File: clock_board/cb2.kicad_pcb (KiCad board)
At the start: 2 copper layers, 110.5 x 38.1 mm, 42 parts, among them IC1 ATMEGA328-P, P1 POWER, P2 PROGRAMMER, P3 BATT_CONN, P4 LEDB_POWER, P5 LCD_CLK_CONN, P6 DIGIT_POWER, Q1 DGT1, Q2 DGT2, Q3 DGT3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

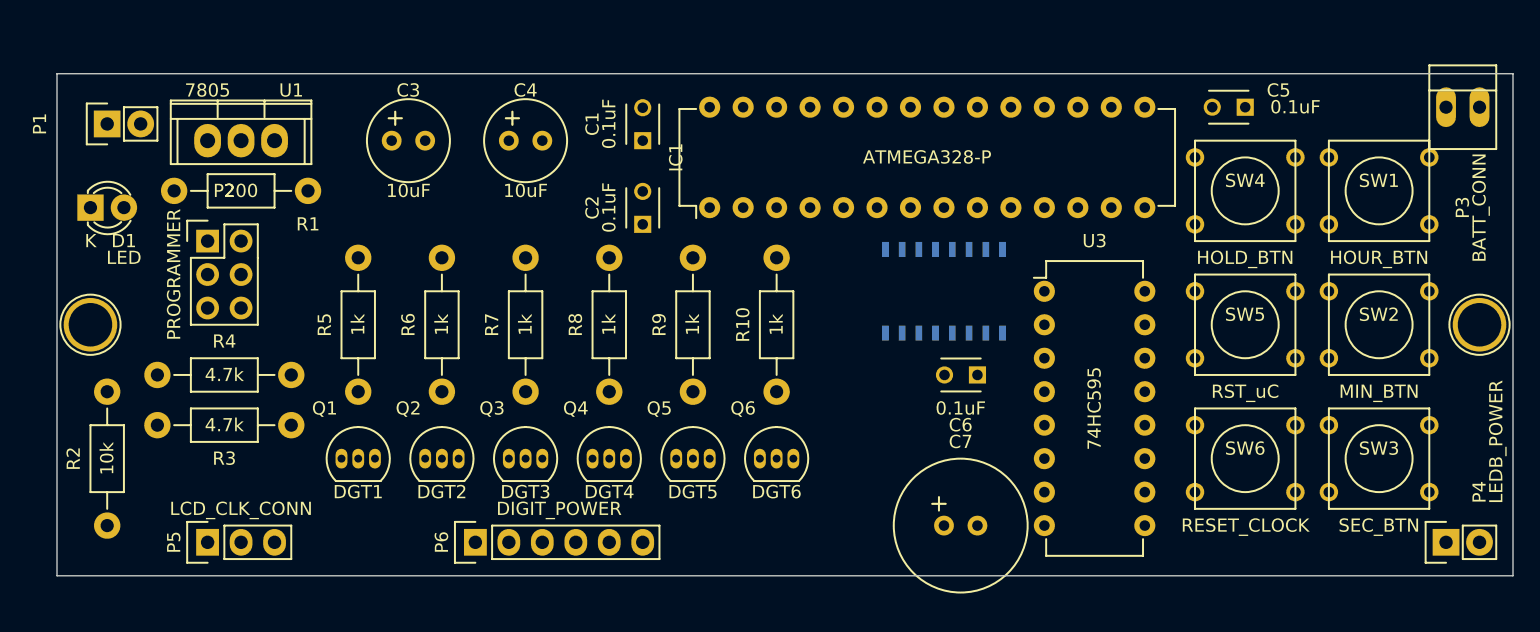
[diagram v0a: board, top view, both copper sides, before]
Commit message: Removed clock reset button.  Improved PCB layout.
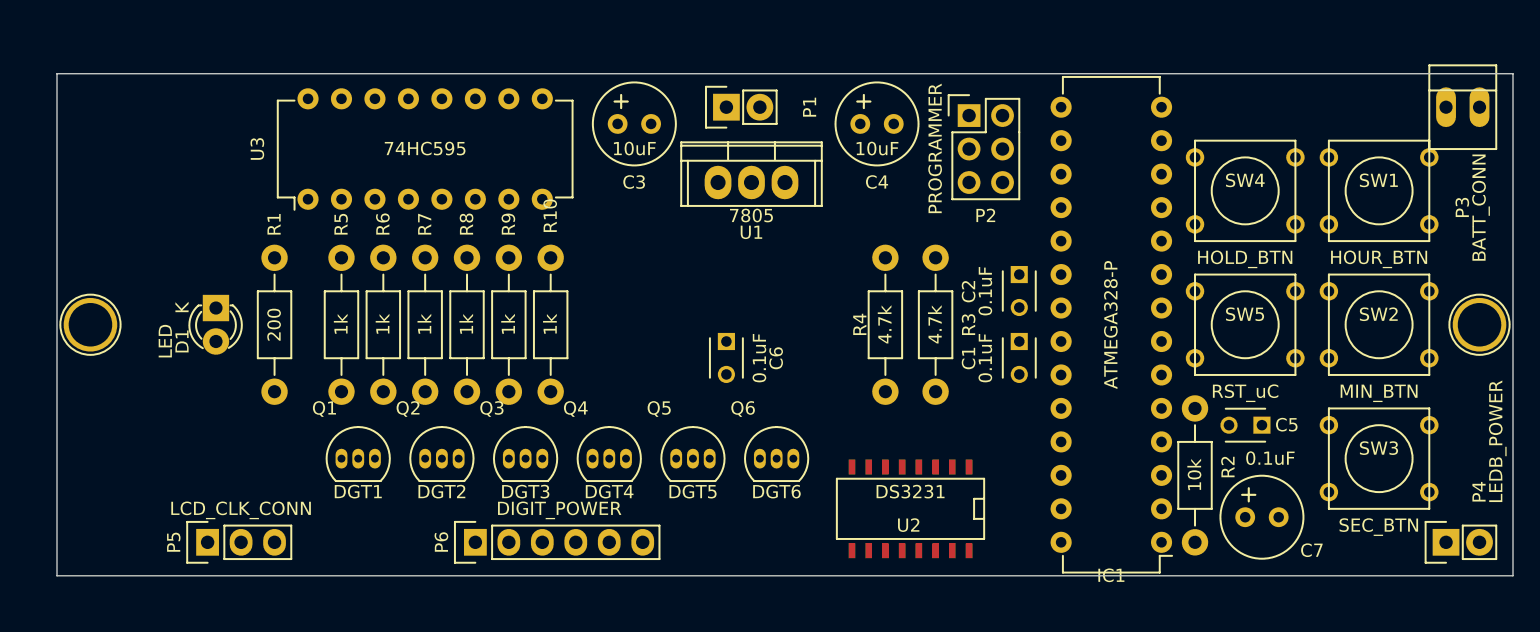
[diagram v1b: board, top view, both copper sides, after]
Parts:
- removed SW6: RESET_CLOCK, Buttons_Switches_ThroughHole:SW_PUSH_SMALL
- C7: footprint Capacitors_Elko_ThroughHole:Elko_vert_20x10mm_RM2.5 -> Capacitors_Elko_ThroughHole:Elko_vert_11.2x6.3mm_RM2.5
- U2: moved to F.Cu
- moved R2 82.6 mm to (152.4, 132.1), turned to 270 degrees
- moved P2 58.6 mm to (135.3, 104.8)
- moved U3 56.3 mm to (85.1, 111.1), turned to 90 degrees
- moved R4 54.1 mm to (132.7, 120.7), turned to 270 degrees
- moved R3 50.7 mm to (128.9, 120.7), turned to 270 degrees
- moved P1 47.0 mm to (116.8, 104.1)
- moved IC1 42.7 mm to (149.9, 137.2), turned to 180 degrees
- moved U1 38.9 mm to (118.7, 109.9)
- moved C1 32.4 mm to (139.1, 121.9), turned to 270 degrees
- moved C2 28.8 mm to (139.1, 116.8), turned to 270 degrees
- moved C4 26.7 mm to (127.0, 105.4)
- moved C5 24.2 mm to (157.5, 128.3)
- moved C7 22.9 mm to (156.2, 135.3)
- moved C6 19.2 mm to (116.8, 121.9), turned to 270 degrees
- moved C3 17.2 mm to (108.6, 105.4)
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
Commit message: Updated footprints for DS3231, 4.7k resistors, and battery connection.
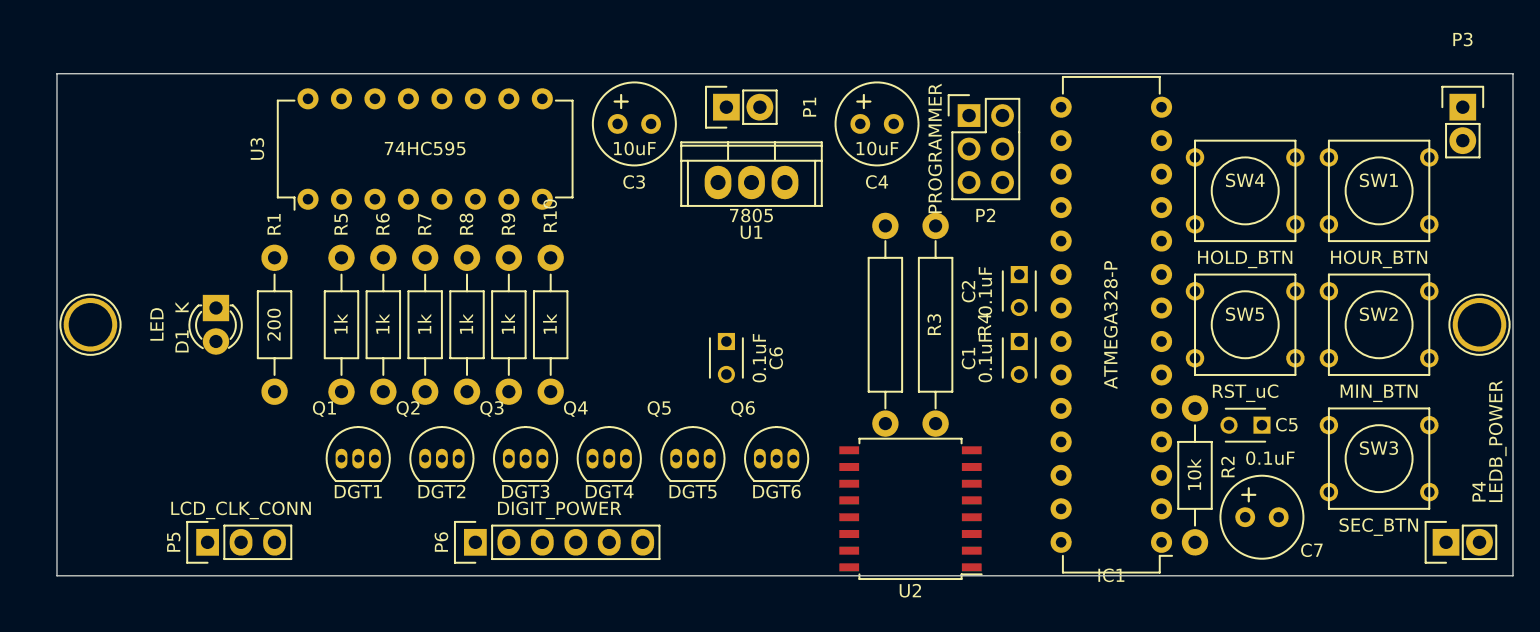
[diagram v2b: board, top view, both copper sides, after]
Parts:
- P3: footprint Connect:PINHEAD1-2 -> Pin_Headers:Pin_Header_Straight_1x02
- R3, R4: footprint Resistors_ThroughHole:Resistor_Horizontal_RM10mm -> Resistors_ThroughHole:Resistor_Horizontal_RM15mm
- U2: footprint SMD_Packages:SO-16-N -> Housings_SOIC:SOIC-16_7.5x10.3mm_Pitch1.27mm

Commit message: Clock board Rev A with routing and placement.
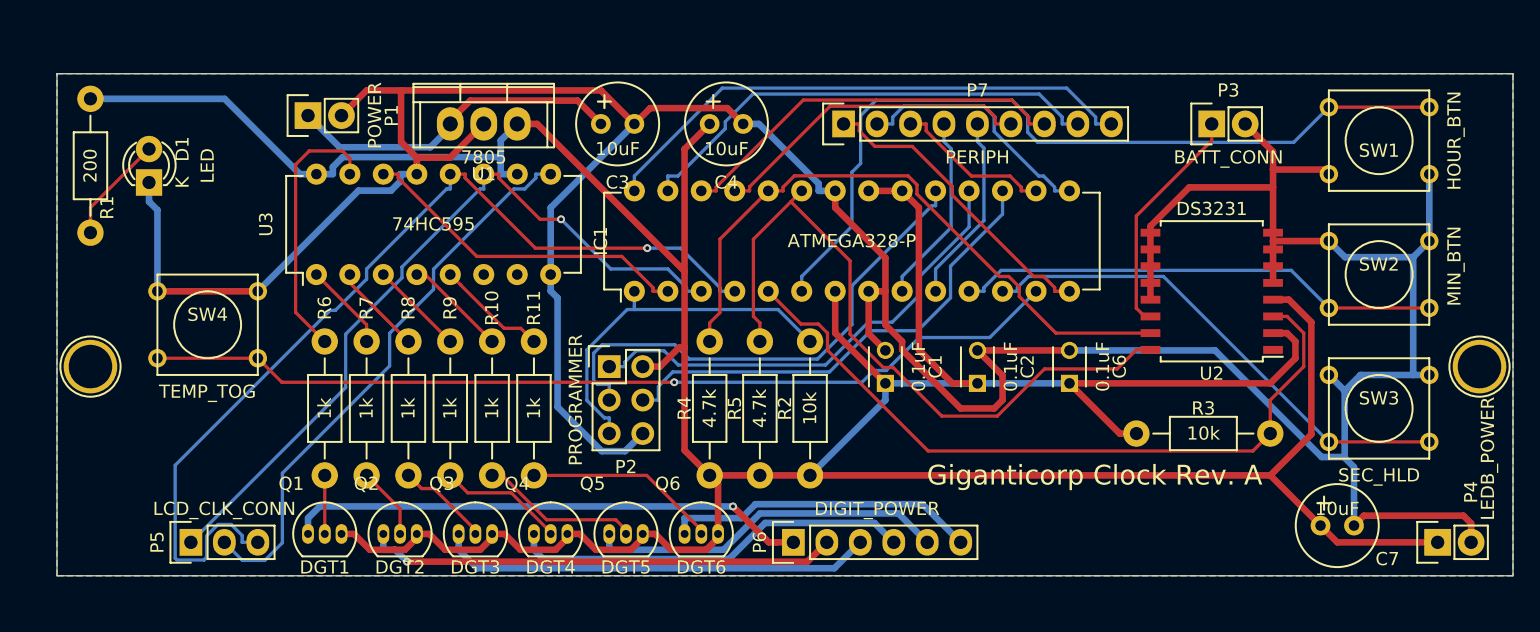
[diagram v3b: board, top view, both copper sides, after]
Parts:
- removed C5: 0.1uF, Capacitors_ThroughHole:C_Disc_D3_P2.5
- removed SW5: RST_uC, Buttons_Switches_ThroughHole:SW_PUSH_SMALL
- added P7: PERIPH, Pin_Headers:Pin_Header_Straight_1x09, F.Cu at (125.7, 105.4)
- added R11: 1k, Resistors_ThroughHole:Resistor_Horizontal_RM10mm, F.Cu at (102.2, 127.0)
- R3: value 4.7k -> 10k; footprint Resistors_ThroughHole:Resistor_Horizontal_RM15mm -> Resistors_ThroughHole:Resistor_Horizontal_RM10mm
- R4: footprint Resistors_ThroughHole:Resistor_Horizontal_RM15mm -> Resistors_ThroughHole:Resistor_Horizontal_RM10mm
- R5: value 1k -> 4.7k
- SW3: value SEC_BTN -> SEC_HLD
- SW4: value HOLD_BTN -> TEMP_TOG
- moved SW4 79.4 mm to (77.5, 120.7)
- moved IC1 44.3 mm to (109.9, 118.1), turned to 90 degrees
- moved P2 33.3 mm to (108.0, 123.8)
- moved R5 32.4 mm to (119.4, 127.0)
- moved P1 31.8 mm to (85.1, 104.8)
- moved R2 29.6 mm to (123.2, 127.0), turned to 90 degrees
- moved U2 28.2 mm to (153.7, 118.1)
- moved C6 26.2 mm to (142.9, 125.1), turned to 90 degrees
- moved R3 25.5 mm to (153.0, 128.9), turned to 180 degrees
- moved P6 24.1 mm to (121.9, 137.2)
- moved U1 20.8 mm to (98.4, 105.4)
- moved P3 19.1 mm to (153.7, 105.4), turned to 90 degrees
- moved R1 18.5 mm to (68.6, 108.6)
- moved R4 18.3 mm to (115.6, 127.0), turned to 90 degrees
- moved C4 11.4 mm to (115.6, 105.4)
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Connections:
- Q1 pad 1: Net-(Q1-Pad1) -> /DIG1
- Q1 pad 2: PROG_VCC -> Net-(Q1-Pad2)
- Q1 pad 3: /DIG1 -> PROG_VCC
- Q2 pad 1: Net-(Q2-Pad1) -> /DIG2
- Q2 pad 2: PROG_VCC -> Net-(Q2-Pad2)
- Q2 pad 3: /DIG2 -> PROG_VCC
- Q3 pad 1: Net-(Q3-Pad1) -> /DIG3
- Q3 pad 2: PROG_VCC -> Net-(Q3-Pad2)
- Q3 pad 3: /DIG3 -> PROG_VCC
- Q4 pad 1: Net-(Q4-Pad1) -> /DIG4
- Q4 pad 2: PROG_VCC -> Net-(Q4-Pad2)
- Q4 pad 3: /DIG4 -> PROG_VCC
- Q5 pad 1: Net-(Q5-Pad1) -> /DIG5
- Q5 pad 2: PROG_VCC -> Net-(Q5-Pad2)
- Q5 pad 3: /DIG5 -> PROG_VCC
- Q6 pad 1: Net-(Q6-Pad1) -> /DIG6
- Q6 pad 2: PROG_VCC -> Net-(Q6-Pad2)
- Q6 pad 3: /DIG6 -> PROG_VCC
- R10 pad 1: Net-(Q6-Pad1) -> Net-(Q5-Pad2)
- R3 pad 1: PROG_VCC -> Net-(IC1-Pad5)
- R3 pad 2: I2C_DATA -> PROG_VCC
- R4 pad 2: I2C_CLK -> I2C_DATA
- R5 pad 1: Net-(Q1-Pad1) -> PROG_VCC
- R5 pad 2: Net-(R5-Pad2) -> I2C_CLK
- R6 pad 1: Net-(Q2-Pad1) -> Net-(Q1-Pad2)
- R7 pad 1: Net-(Q3-Pad1) -> Net-(Q2-Pad2)
- R8 pad 1: Net-(Q4-Pad1) -> Net-(Q3-Pad2)
- R9 pad 1: Net-(Q5-Pad1) -> Net-(Q4-Pad2)
- SW1 pad 2: Net-(IC1-Pad5) -> Net-(IC1-Pad6)
- U2 pad 1: Net-(IC1-Pad6) -> Net-(U2-Pad1)
- U2 pad 3: Net-(U2-Pad3) -> Net-(IC1-Pad5)
- U3 pad 1: Net-(R6-Pad2) -> Net-(R7-Pad2)
- U3 pad 15: Net-(R5-Pad2) -> Net-(R6-Pad2)
- U3 pad 2: Net-(R7-Pad2) -> Net-(R8-Pad2)
- U3 pad 3: Net-(R8-Pad2) -> Net-(R9-Pad2)
- U3 pad 4: Net-(R9-Pad2) -> Net-(R10-Pad2)
- U3 pad 5: Net-(R10-Pad2) -> Net-(R11-Pad2)
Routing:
- net PROG_VCC: track 0.00 -> 282.7 mm
- net PROG_GND: track 0.00 -> 276.9 mm
- net SDL: track 0.00 -> 73.1 mm, vias 0 -> 1
- net Net-(IC1-Pad13): track 0.00 -> 70.3 mm, vias 0 -> 1
- net Net-(IC1-Pad6): track 0.00 -> 62.0 mm
- net CLK: track 0.00 -> 57.8 mm, vias 0 -> 1
- net Net-(IC1-Pad5): track 0.00 -> 56.0 mm
- net I2C_CLK: track 0.00 -> 52.5 mm
- net I2C_DATA: track 0.00 -> 48.7 mm
- net Net-(P5-Pad2): track 0.00 -> 43.1 mm
- net Net-(IC1-Pad28): track 0.00 -> 41.5 mm
- net /DIG1: track 0.00 -> 39.5 mm, vias 0 -> 1
- net PROG_SCK: track 0.00 -> 38.9 mm
- net Net-(IC1-Pad12): track 0.00 -> 38.2 mm
- net PROG_MOSI: track 0.00 -> 36.9 mm
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- added copper zone on B.Cu, net PROG_GND
- added copper zone on F.Cu, net PROG_GND
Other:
- board text added: "Giganticorp Clock Rev. A"
